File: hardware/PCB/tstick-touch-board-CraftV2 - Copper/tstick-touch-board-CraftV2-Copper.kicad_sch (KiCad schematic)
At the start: 12 parts, among them J1 Conn_01x32, U1 Trill_Craft

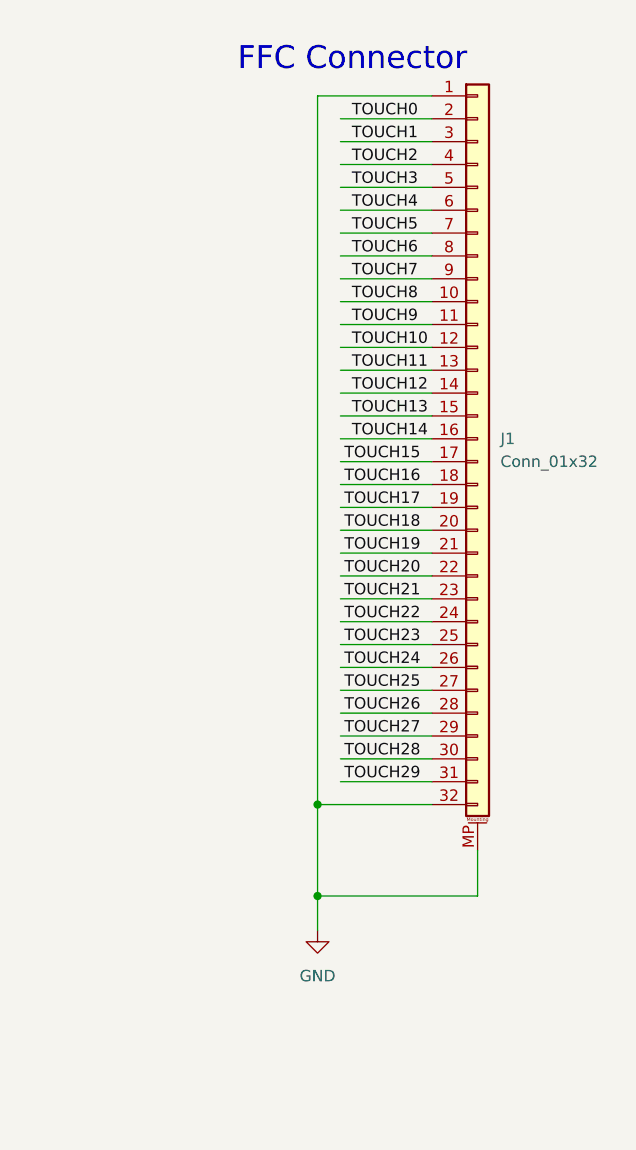
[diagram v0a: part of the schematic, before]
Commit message: fixed errors in schematic, added support for V1 Trill boards in v2 board design, changed headers to vertical headers in touch board
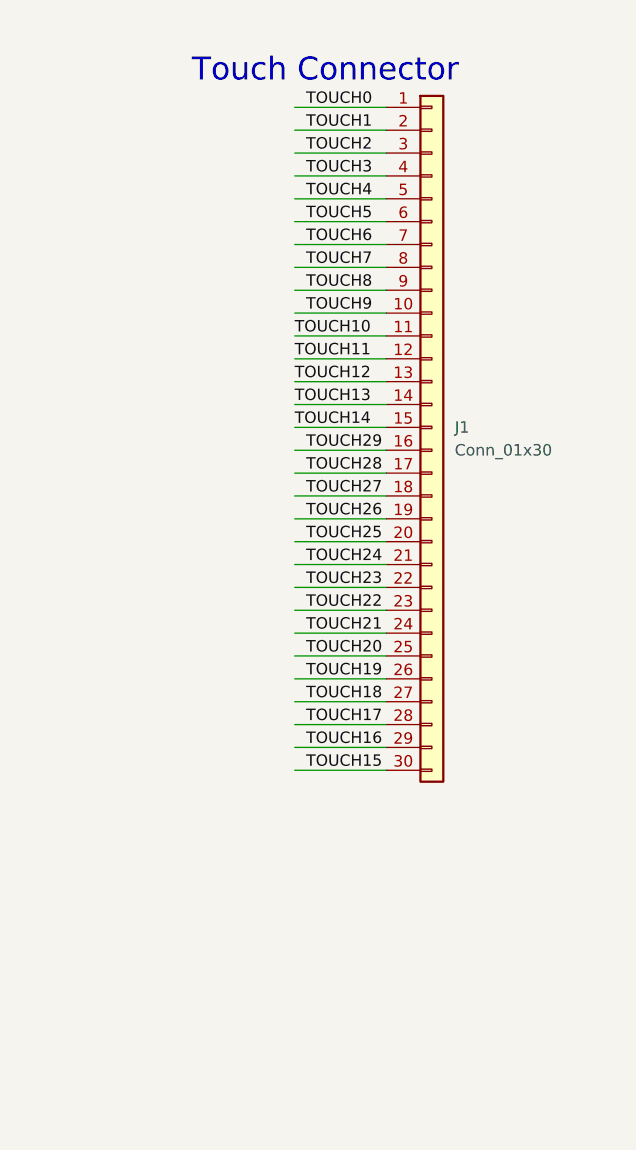
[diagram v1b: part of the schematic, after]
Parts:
- removed J1: Conn_01x32, ffc_footprints:CON_541323262_MOL, symbol Connector_Generic_MountingPin:Conn_01x32_MountingPin
- added J1: Conn_01x30, touch-sensors:tstick-buttons, symbol Connector_Generic:Conn_01x30
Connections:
- net TOUCH0: now also J1.1 (Pin_1)
- net TOUCH1: now also J1.2 (Pin_2)
- net TOUCH10: now also J1.11 (Pin_11)
- net TOUCH11: now also J1.12 (Pin_12)
- net TOUCH12: now also J1.13 (Pin_13)
- net TOUCH13: now also J1.14 (Pin_14)
- net TOUCH14: now also J1.15 (Pin_15)
- net TOUCH15: now also J1.30 (Pin_30)
- net TOUCH16: now also J1.29 (Pin_29)
- net TOUCH17: now also J1.28 (Pin_28)
- net TOUCH18: now also J1.27 (Pin_27)
- net TOUCH19: now also J1.26 (Pin_26)
- net TOUCH2: now also J1.3 (Pin_3)
- net TOUCH20: now also J1.25 (Pin_25)
- net TOUCH21: now also J1.24 (Pin_24)
- net TOUCH22: now also J1.23 (Pin_23)
- net TOUCH23: now also J1.22 (Pin_22)
- net TOUCH24: now also J1.21 (Pin_21)
- net TOUCH25: now also J1.20 (Pin_20)
- net TOUCH26: now also J1.19 (Pin_19)
- net TOUCH27: now also J1.18 (Pin_18)
- net TOUCH28: now also J1.17 (Pin_17)
- net TOUCH29: now also J1.16 (Pin_16)
- net TOUCH3: now also J1.4 (Pin_4)
- net TOUCH4: now also J1.5 (Pin_5)
- net TOUCH5: now also J1.6 (Pin_6)
- net TOUCH6: now also J1.7 (Pin_7)
- net TOUCH7: now also J1.8 (Pin_8)
- net TOUCH8: now also J1.9 (Pin_9)
- net TOUCH9: now also J1.10 (Pin_10)
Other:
- note added: "Touch Connector"
- note removed: "FFC Connector"
